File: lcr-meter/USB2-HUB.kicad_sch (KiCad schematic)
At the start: 32 parts, among them J11 USB_OTG, J13 690-008-221-904, J14 Conn_02x05_Odd_Even, U13 FSUSB42MUX, U4 TPD4EUSB30, U6 USB2514B-I/M2, U7 AP22653W6, Y1 24MHz

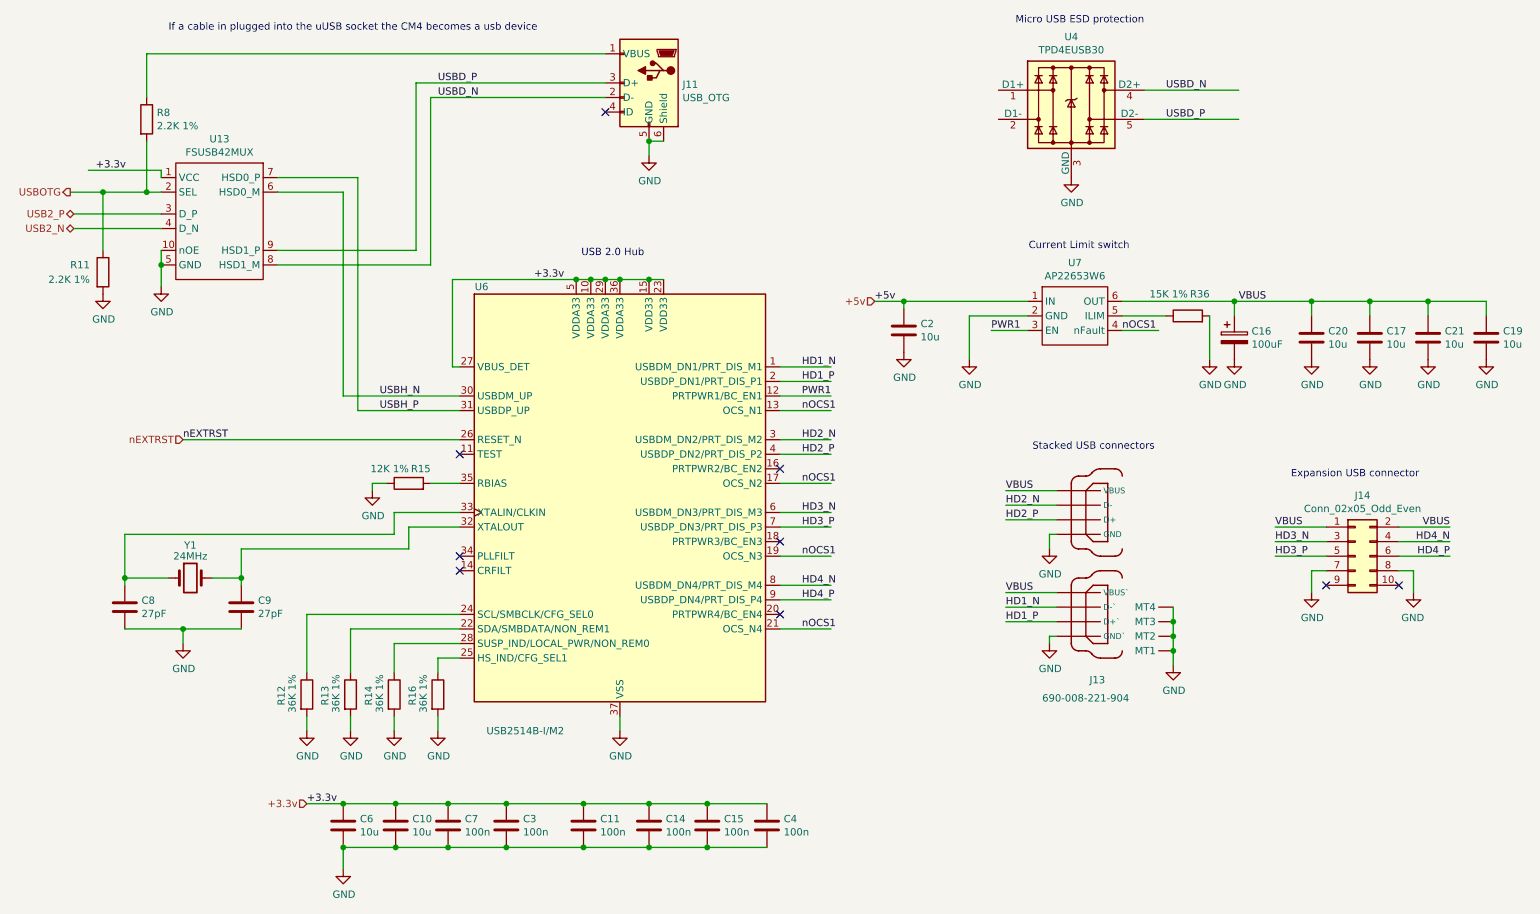
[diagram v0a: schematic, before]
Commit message: Addressable LED test board
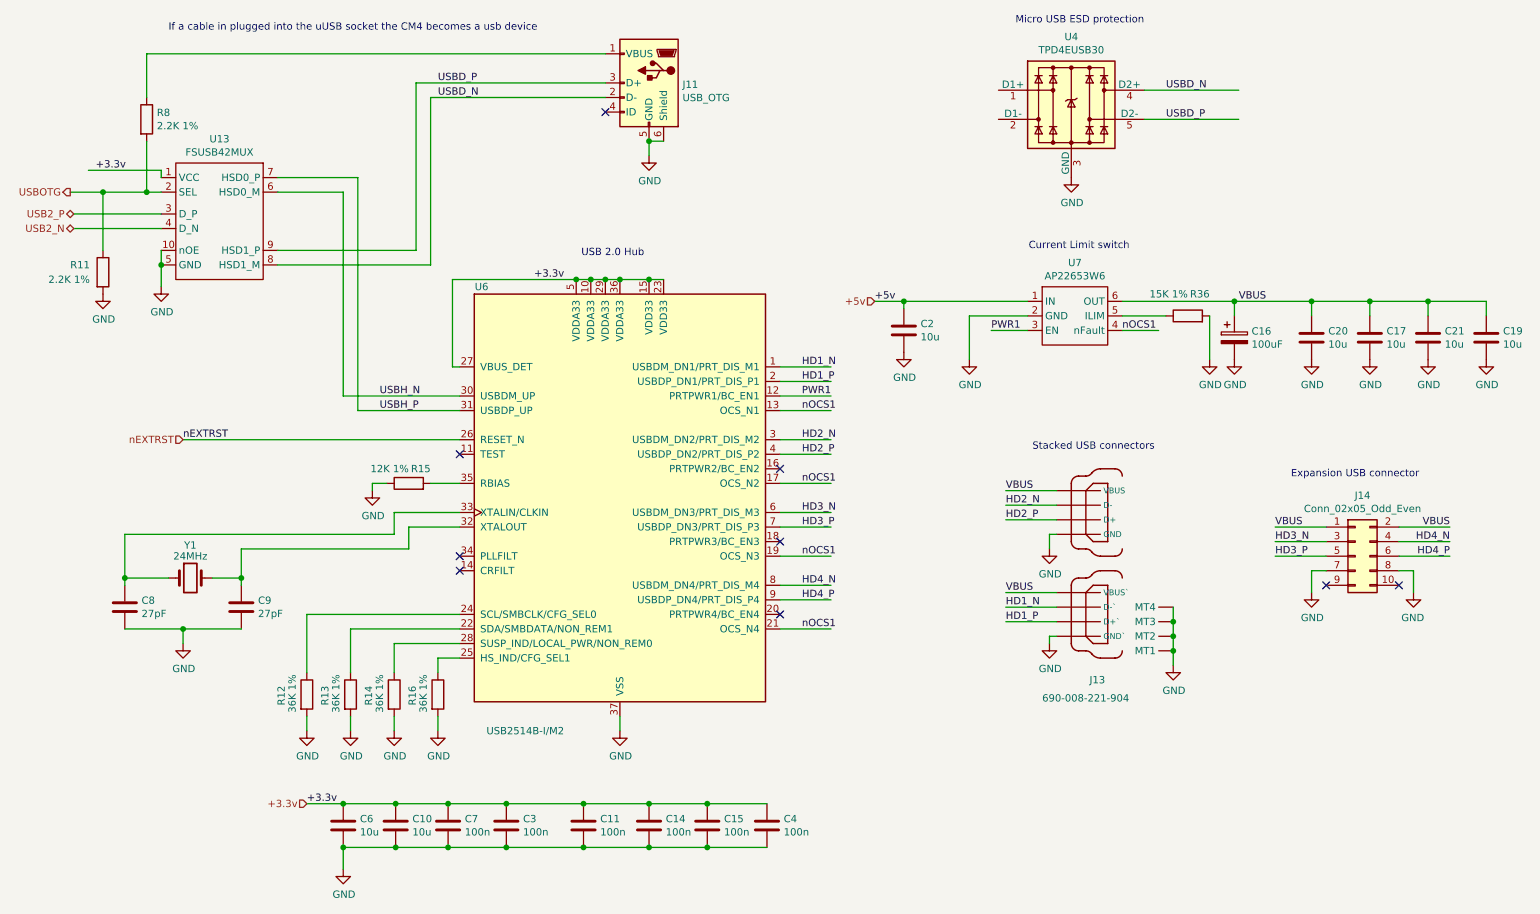
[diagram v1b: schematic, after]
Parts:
- J13: Field5 2751688 -> 2751688; Field6 690-008-221-904 -> None; Field7 EDAC -> Molex; Field8 UCON00727 -> None
- U7: Field5 31-AP22653W6-7CT-ND -> AP2553W6-7DICT-ND
